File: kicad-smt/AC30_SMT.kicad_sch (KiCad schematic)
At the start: 81 parts, among them IC10 555, IC11 4001, IC12 1489, IC13 4070, IC14 4053, IC15 1488, IC6 4053, IC7 4049, IC8 4013, IC9 4023, J1 Front panel harness 1, J10 MOTOR A, J11 MOTOR B, J2 Front panel harness 2, J3 Computer interface (COMP), J4 Control interface, J5 Terminal interface (TERM), J6 MIC A, J7 MIC B, J8 EAR A, J9 EAR B, Q10 MMBT5087, Q11 MMBT5087, Q5 MMBT5088, Q6 MMBT5088, Q7 MMBT5088, Q8 MMBT5088, Q9 MMBT5087

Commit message: SMT board: through-hole jumper pads for the front panel
Replace the J1/J2 KK-396 front-panel harness headers on the SMT board with
five rows of 0.1 in through-hole wire pads along the bottom edge, each pad
labelled with its net name on the silkscreen:
J1 SWITCHES, J2 LEDS, J13 MOTOR, J14 MIC (AUDIO_OUT), J15 EAR (AUDIO_IN).

The through-hole board keeps J1/J2. SMT board is now 173.0 x 89.0 mm;
ERC, DRC (all severities) and parity clean, fully routed.
AC30-SMT-settings.md updated.

Co-Authored-By: Claude Opus 5.5 <noreply@anthropic.com>
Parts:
- added J13: MOTOR, Connector_PinHeader_2.54mm:PinHeader_1x04_P2.54mm_Vertical, symbol Connector_Generic:Conn_01x04
- added J14: MIC, Connector_PinHeader_2.54mm:PinHeader_1x02_P2.54mm_Vertical, symbol Connector_Generic:Conn_01x02
- added J15: EAR, Connector_PinHeader_2.54mm:PinHeader_1x02_P2.54mm_Vertical, symbol Connector_Generic:Conn_01x02
- J1: value Front panel harness 1 -> SWITCHES; footprint Connector_Molex:Molex_KK-396_A-41791-0015_1x15_P3.96mm_Vertical -> Connector_PinHeader_2.54mm:PinHeader_1x13_P2.54mm_Vertical; symbol Connector_Generic:Conn_01x15 -> Connector_Generic:Conn_01x13
- J2: value Front panel harness 2 -> LEDS; footprint Connector_Molex:Molex_KK-396_A-41791-0012_1x12_P3.96mm_Vertical -> Connector_PinHeader_2.54mm:PinHeader_1x05_P2.54mm_Vertical; symbol Connector_Generic:Conn_01x12 -> Connector_Generic:Conn_01x05
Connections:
- net +5V: now also J1.1 (Pin_1), J2.1 (Pin_1); no longer J1.2 (Pin_2)
- net AUDIO_IN: now also J15.1 (Pin_1); no longer J2.8 (Pin_8)
- net AUDIO_OUT: now also J14.1 (Pin_1); no longer J2.7 (Pin_7)
- net CARRIER_EN_N: now also J1.3 (Pin_3); no longer J2.9 (Pin_9)
- net GND: now also J1.2 (Pin_2), J14.2 (Pin_2), J15.2 (Pin_2); no longer J1.4 (Pin_4), J2.10 (Pin_10)
- net LED_READ_DATA: now also J2.5 (Pin_5); no longer J1.3 (Pin_3)
- net LED_READ_RDY: now also J2.3 (Pin_3); no longer J2.5 (Pin_5)
- net LED_REC_DATA: now also J2.4 (Pin_4); no longer J1.6 (Pin_6)
- net LED_REC_RDY: now also J2.2 (Pin_2); no longer J2.6 (Pin_6)
- net LOCAL_REMOTE: now also J1.9 (Pin_9); no longer J1.8 (Pin_8)
- net MAN_MOTOR: now also J1.4 (Pin_4); no longer J1.11 (Pin_11)
- net MOTOR_1A: now also J13.1 (Pin_1); no longer J1.1 (Pin_1)
- net MOTOR_1B: now also J13.2 (Pin_2); no longer J1.7 (Pin_7)
- net MOTOR_2A: now also J13.3 (Pin_3); no longer J1.14 (Pin_14)
- net MOTOR_2B: now also J13.4 (Pin_4); no longer J2.1 (Pin_1)
- net READ_RLY_DRV: now also J1.11 (Pin_11); no longer J1.12 (Pin_12)
- net READ_RST: now also J1.8 (Pin_8); no longer J1.9 (Pin_9)
- net READ_SET: now also J1.7 (Pin_7); no longer J2.2 (Pin_2)
- net REC_RST: now also J1.6 (Pin_6); no longer J2.4 (Pin_4)
- net REC_SET: now also J1.5 (Pin_5); no longer J2.3 (Pin_3)
- net RELAY_1: now also J1.12 (Pin_12); no longer J1.5 (Pin_5)
- no-connect marks 38 -> 35
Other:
- note added: "Front panel jumper pads"
- moved on the sheet: C12, C13, C14, C15, C16, C17, C18, C19, C20, D10, D11, D18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

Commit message: SMT board: separate MIC A/B and EAR A/B jumper pads
Each front-panel jack now has its own tip and GND pads (J14 MIC: MIC_A,
GND, MIC_B, GND; J15 EAR: EAR_A, GND, EAR_B, GND). The S2/S3 audio poles
wire to new SWITCHES pads (AUDIO_OUT, MIC_A/B, AUDIO_IN, EAR_A/B) and the
board joins them. SMT board is now 173.0 x 88.5 mm; ERC, DRC (all
severities) and parity clean, fully routed. AC30-SMT-settings.md updated.

Co-Authored-By: Claude Opus 5.5 <noreply@anthropic.com>
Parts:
- J1: footprint Connector_PinHeader_2.54mm:PinHeader_1x13_P2.54mm_Vertical -> Connector_PinHeader_2.54mm:PinHeader_1x19_P2.54mm_Vertical; symbol Connector_Generic:Conn_01x13 -> Connector_Generic:Conn_01x19
- J14, J15: footprint Connector_PinHeader_2.54mm:PinHeader_1x02_P2.54mm_Vertical -> Connector_PinHeader_2.54mm:PinHeader_1x04_P2.54mm_Vertical; symbol Connector_Generic:Conn_01x02 -> Connector_Generic:Conn_01x04
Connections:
- net AUDIO_IN: now also J1.17 (Pin_17); no longer J15.1 (Pin_1)
- net AUDIO_OUT: now also J1.10 (Pin_10); no longer J14.1 (Pin_1)
- net EAR_A: now also J1.18 (Pin_18), J15.1 (Pin_1)
- net EAR_B: now also J1.19 (Pin_19), J15.3 (Pin_3)
- net GND: now also J14.4 (Pin_4), J15.4 (Pin_4)
- net MIC_A: now also J1.11 (Pin_11), J14.1 (Pin_1)
- net MIC_B: now also J1.12 (Pin_12), J14.3 (Pin_3)
- net READ_RLY_DRV: now also J1.16 (Pin_16); no longer J1.11 (Pin_11)
- net REC_RLY_DRV: now also J1.13 (Pin_13); no longer J1.10 (Pin_10)
- net RELAY_1: now also J1.14 (Pin_14); no longer J1.12 (Pin_12)
- net RELAY_2: now also J1.15 (Pin_15); no longer J1.13 (Pin_13)
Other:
- moved on the sheet: C12, C13, C14, C15, C16, C17, C18, C19, C20, D10, D11, D18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

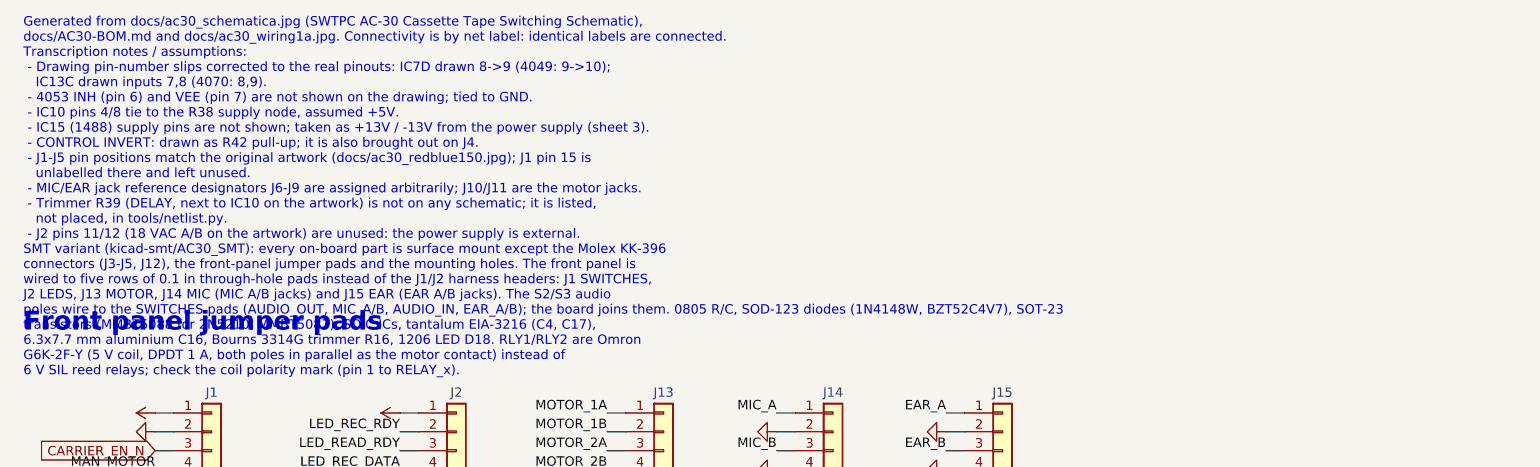
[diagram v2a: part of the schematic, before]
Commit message: Through-hole board: front-panel jumper pads in place of J1/J2
Both boards now wire the front panel to five rows of 0.1 in through-hole
pads with net names on the silkscreen (J1 SWITCHES, J2 LEDS, J13 MOTOR,
J14 MIC, J15 EAR) instead of the artwork's J1/J2 KK-396 headers.

The through-hole build weights board height at 60 (AC30_HEIGHT_W) so the
bottom row doesn't stretch the board; it is now 173.0 x 126.5 mm, fully
routed, ERC/DRC/parity clean. SMT board unchanged apart from symbol IDs
and the schematic note. AC30-settings.md updated.

Co-Authored-By: Claude Opus 5.5 <noreply@anthropic.com>
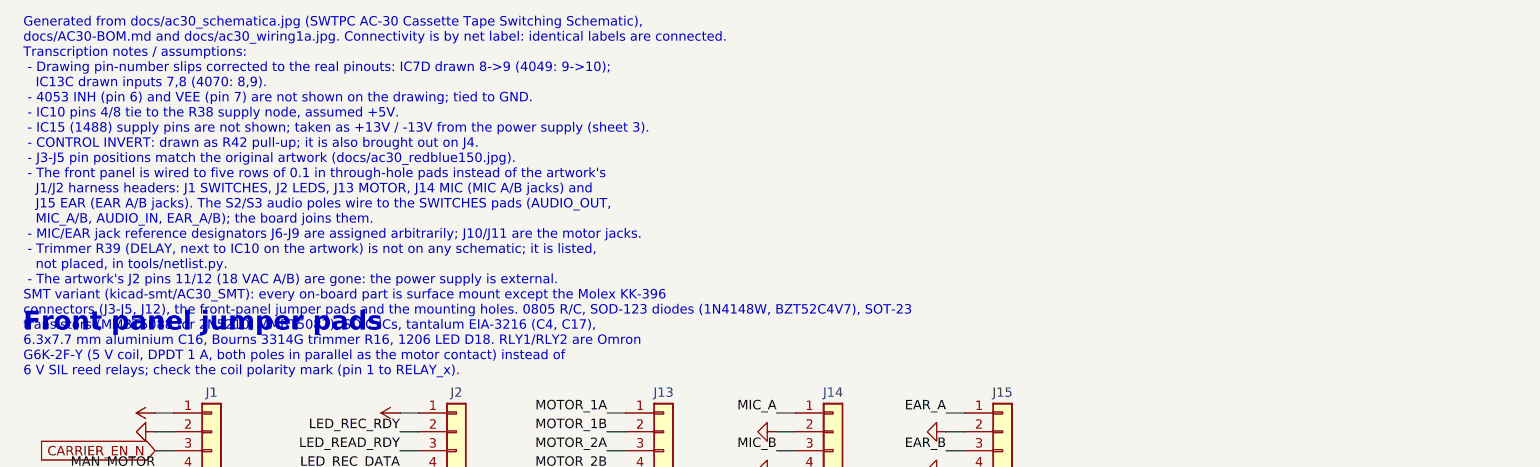
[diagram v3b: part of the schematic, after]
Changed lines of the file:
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@@
 		)
 	)
-	(text "Generated from docs/ac30_schematica.jpg (SWTPC AC-30 Cassette Tape Switching Schematic),\ndocs/AC30-BOM.md and docs/ac30_wiring1a.jpg. Connectivity is by net label: identical labels are connected.\nTranscription notes / assumptions:\n - Drawing pin-number slips corrected to the real pinouts: IC7D drawn 8->9 (4049: 9->10);\n   IC13C drawn inputs 7,8 (4070: 8,9).\n - 4053 INH (pin 6) and VEE (pin 7) are not shown on the drawing; tied to GND.\n - IC10 pins 4/8 tie to the R38 supply node, assumed +5V.\n - IC15 (1488) supply pins are not shown; taken as +13V / -13V from the power supply (sheet 3).\n - CONTROL INVERT: drawn as R42 pull-up; it is also brought out on J4.\n - J1-J5 pin positions match the original artwork (docs/ac30_redblue150.jpg); J1 pin 15 is\n   unlabelled there and left unused.\n - MIC/EAR jack reference designators J6-J9 are assigned arbitrarily; J10/J11 are the motor jacks.\n - Trimmer R39 (DELAY, next to IC10 on the artwork) is not on any schematic; it is listed,\n   not placed, in tools/netlist.py.\n - J2 pins 11/12 (18 VAC A/B on the artwork) are unused: the power supply is external.\nSMT variant (kicad-smt/AC30_SMT): every on-board part is surface mount except the Molex KK-396\nconnectors (J3-J5, J12), the front-panel jumper pads and the mounting holes. The front panel is\nwired to five rows of 0.1 in through-hole pads instead of the J1/J2 harness headers: J1 SWITCHES,\nJ2 LEDS, J13 MOTOR, J14 MIC (MIC A/B jacks) and J15 EAR (EAR A/B jacks). The S2/S3 audio\npoles wire to the SWITCHES pads (AUDIO_OUT, MIC_A/B, AUDIO_IN, EAR_A/B); the board joins them. 0805 R/C, SOD-123 diodes (1N4148W, BZT52C4V7), SOT-23\ntransistors (MMBT5088 for 2N5210, MMBT5087), SOIC ICs, tantalum EIA-3216 (C4, C17),\n6.3x7.7 mm aluminium C16, Bourns 3314G trimmer R16, 1206 LED D18. RLY1/RLY2 are Omron\nG6K-2F-Y (5 V coil, DPDT 1 A, both poles in parallel as the motor contact) instead of\n6 V SIL reed relays; check the coil polarity mark (pin 1 to RELAY_x)."
+	(text "Generated from docs/ac30_schematica.jpg (SWTPC AC-30 Cassette Tape Switching Schematic),\ndocs/AC30-BOM.md and docs/ac30_wiring1a.jpg. Connectivity is by net label: identical labels are connected.\nTranscription notes / assumptions:\n - Drawing pin-number slips corrected to the real pinouts: IC7D drawn 8->9 (4049: 9->10);\n   IC13C drawn inputs 7,8 (4070: 8,9).\n - 4053 INH (pin 6) and VEE (pin 7) are not shown on the drawing; tied to GND.\n - IC10 pins 4/8 tie to the R38 supply node, assumed +5V.\n - IC15 (1488) supply pins are not shown; taken as +13V / -13V from the power supply (sheet 3).\n - CONTROL INVERT: drawn as R42 pull-up; it is also brought out on J4.\n - J3-J5 pin positions match the original artwork (docs/ac30_redblue150.jpg).\n - The front panel is wired to five rows of 0.1 in through-hole pads instead of the artwork's\n   J1/J2 harness headers: J1 SWITCHES, J2 LEDS, J13 MOTOR, J14 MIC (MIC A/B jacks) and\n   J15 EAR (EAR A/B jacks). The S2/S3 audio poles wire to the SWITCHES pads (AUDIO_OUT,\n   MIC_A/B, AUDIO_IN, EAR_A/B); the board joins them.\n - MIC/EAR jack reference designators J6-J9 are assigned arbitrarily; J10/J11 are the motor jacks.\n - Trimmer R39 (DELAY, next to IC10 on the artwork) is not on any schematic; it is listed,\n   not placed, in tools/netlist.py.\n - The artwork's J2 pins 11/12 (18 VAC A/B) are gone: the power supply is external.\nSMT variant (kicad-smt/AC30_SMT): every on-board part is surface mount except the Molex KK-396\nconnectors (J3-J5, J12), the front-panel jumper pads and the mounting holes. 0805 R/C, SOD-123 diodes (1N4148W, BZT52C4V7), SOT-23\ntransistors (MMBT5088 for 2N5210, MMBT5087), SOIC ICs, tantalum EIA-3216 (C4, C17),\n6.3x7.7 mm aluminium C16, Bourns 3314G trimmer R16, 1206 LED D18. RLY1/RLY2 are Omron\nG6K-2F-Y (5 V coil, DPDT 1 A, both poles in parallel as the motor contact) instead of\n6 V SIL reed relays; check the coil polarity mark (pin 1 to RELAY_x)."
 		(exclude_from_sim no)
 		(at 20.32 20.32 0)

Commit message: Wired, human-readable schematics with PDF and PNG images
gen.py now lays out each functional group on its own and draws its nets
as real wires (new tools/schroute.py: orthogonal grid router that never
ends, bends or overlaps on another net's wire); every routed net keeps
one label with its name, labels join nets between blocks and sheets, and
unroutable connections fall back to label pairs (17). The front-panel
jumper pads share the front-panel block. Custom 1488/1489 output pins
moved onto the 2.54 mm grid.

build.sh exports schematic/<project>.pdf and, via tools/schimg.py, PNGs
of every sheet and functional block for both boards.

Connectivity unchanged (pin-to-net maps identical for both variants);
ERC 0; both PCBs DRC/parity clean and unchanged. Docs updated.

Co-Authored-By: Claude Opus 5.5 <noreply@anthropic.com>
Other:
- note added: "Generated from docs/ac30_schematica.jpg (SWTPC AC-30 Cassette Tape Switching Schematic), docs/AC30-BOM.md and docs/ac30_wiring1a.jpg. Each block is wired; net labels join the blocks and sheets (identical labels are connected). Transcription notes / assumptions: - Drawing pin-number slips corrected to the real pinouts: IC7D drawn 8->9 (4049: 9->10); IC13C drawn inputs 7,8 (4070: 8,9). - 4053 INH (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"
- note removed: "Front panel jumper pads"
- note removed: "Generated from docs/ac30_schematica.jpg (SWTPC AC-30 Cassette Tape Switching Schematic), docs/AC30-BOM.md and docs/ac30_wiring1a.jpg. Connectivity is by net label: identical labels are connected. Transcription notes / assumptions: - Drawing pin-number slips corrected to the real pinouts: IC7D drawn 8->9 (4049: 9->10); IC13C drawn inputs 7,8 (4070: 8,9). - 4053 INH (pin 6) and VEE (pin 7) are not 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"
- moved on the sheet: C12, C13, C14, C15, C16, C17, C18, C19, C20, D10, D11, D18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
